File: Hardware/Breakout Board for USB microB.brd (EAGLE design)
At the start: 20.3 x 11.4 mm, 7 parts

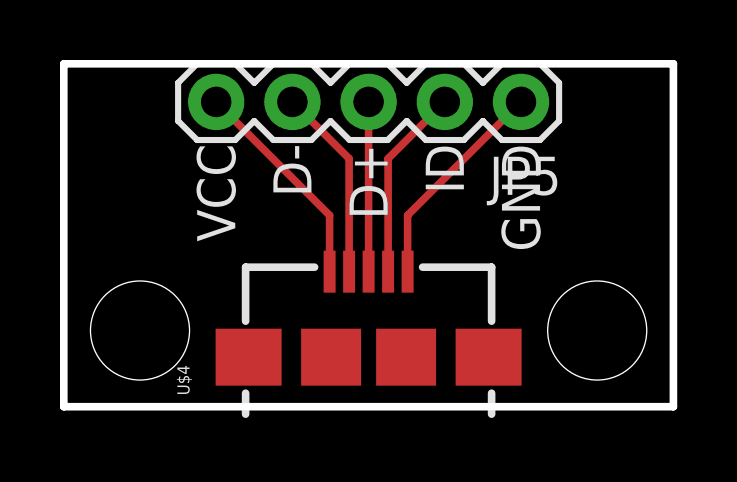
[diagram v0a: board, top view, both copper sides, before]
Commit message: Swapped in new microB FP w/ bosses
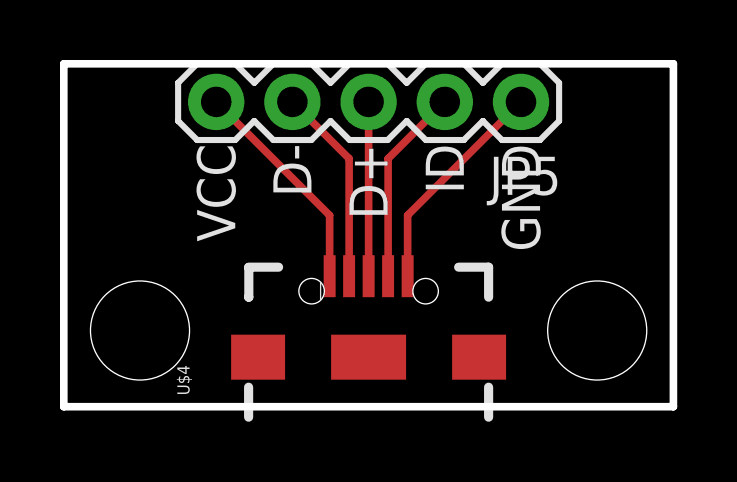
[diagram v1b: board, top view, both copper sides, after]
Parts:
- U$4: value USB_AB -> (none); device SparkFun-Connectors:USB-AB-MICRO-SMD -> Testing:USB-AB-MICRO-SMD_V02_BOSS
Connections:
- net D+: now also U$4.D+1; no longer U$4.D+
- net D-: now also U$4.D-1; no longer U$4.D-
- net GND: now also U$4.GND1; no longer U$4.GND
- net ID: now also U$4.ID1; no longer U$4.ID
- net VBUS: now also U$4.VBUS1; no longer U$4.VBUS

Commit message: Updated board with current FP.
No changes to layout just part value update. Engineering file audit. See
eagle issues for more info.
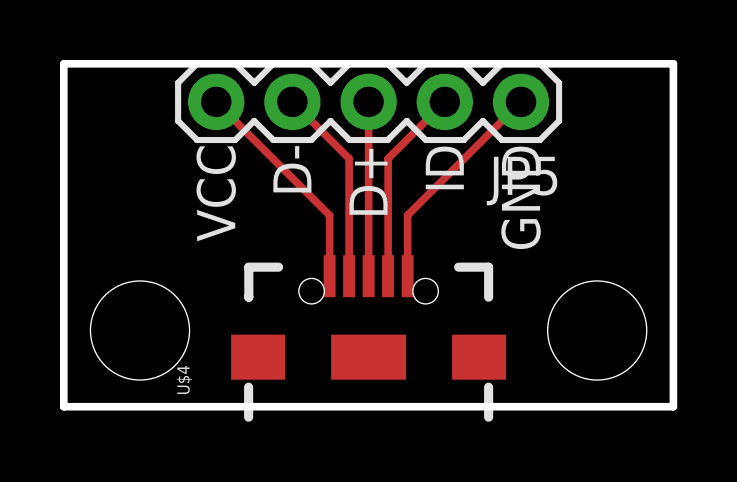
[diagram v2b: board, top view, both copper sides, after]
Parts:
- U$4: device Testing:USB-AB-MICRO-SMD_V02_BOSS -> SparkFun-Connectors:USB-AB-MICRO-SMD_V03
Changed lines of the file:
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@@
 <?xml version="1.0" encoding="utf-8"?>
 <!DOCTYPE eagle SYSTEM "eagle.dtd">
-<eagle version="6.4">
+<eagle version="7.2.0">
 <drawing>
 <settings>
@@
 <layer number="54" name="bGND_GNDA" color="1" fill="9" visible="no" active="no"/>
 <layer number="56" name="wert" color="7" fill="1" visible="no" active="yes"/>
+<layer number="57" name="tCAD" color="7" fill="1" visible="no" active="no"/>
+<layer number="90" name="Modules" color="5" fill="1" visible="no" active="no"/>
 <layer number="91" name="Nets" color="2" fill="1" visible="no" active="no"/>
 <layer number="92" name="Busses" color="1" fill="1" visible="no" active="no"/>
@@
 <layer number="97" name="Info" color="7" fill="1" visible="no" active="no"/>
 <layer number="98" name="Guide" color="6" fill="1" visible="no" active="no"/>
+<layer number="99" name="SpiceOrder" color="7" fill="1" visible="no" active="no"/>
 <layer number="100" name="Muster" color="7" fill="1" visible="no" active="no"/>
 <layer number="101" name="Patch_Top" color="12" fill="4" visible="no" active="yes"/>
@@
 <layer number="108" name="tplace-old" color="10" fill="1" visible="no" active="yes"/>
 <layer number="109" name="ref-old" color="11" fill="1" visible="no" active="yes"/>
+<layer number="110" name="fp0" color="7" fill="1" visible="yes" active="yes"/>
+<layer number="111" name="LPC17xx" color="7" fill="1" visible="yes" active="yes"/>
+<layer number="112" name="tSilk" color="7" fill="1" visible="yes" active="yes"/>
+<layer number="113" name="IDFDebug" color="4" fill="1" visible="yes" active="yes"/>
 <layer number="116" name="Patch_BOT" color="9" fill="4" visible="no" active="yes"/>
 <layer number="121" name="_tsilk" color="7" fill="1" visible="no" active="yes"/>
 <layer number="122" name="_bsilk" color="7" fill="1" visible="no" active="yes"/>
+<layer number="123" name="tTestmark" color="7" fill="1" visible="yes" active="yes"/>
+<layer number="124" name="bTestmark" color="7" fill="1" visible="yes" active="yes"/>
 <layer number="125" name="_tNames" color="7" fill="1" visible="no" active="yes"/>
+<layer number="126" name="_bNames" color="7" fill="1" visible="yes" active="yes"/>
+<layer number="127" name="_tValues" color="7" fill="1" visible="yes" active="yes"/>
+<layer number="128" name="_bValues" color="7" fill="1" visible="yes" active="yes"/>
+<layer number="131" name="tAdjust" color="7" fill="1" visible="yes" active="yes"/>
+<layer number="132" name="bAdjust" color="7" fill="1" visible="yes" active="yes"/>
 <layer number="144" name="Drill_legend" color="7" fill="1" visible="no" active="yes"/>
+<layer number="150" name="Notes" color="7" fill="1" visible="yes" active="yes"/>
 <layer number="151" name="HeatSink" color="7" fill="1" visible="no" active="yes"/>
+<layer number="152" name="_bDocu" color="7" fill="1" visible="yes" active="yes"/>
+<layer number="153" name="FabDoc1" color="7" fill="1" visible="yes" active="yes"/>
+<layer number="154" name="FabDoc2" color="7" fill="1" visible="yes" active="yes"/>
+<layer number="155" name="FabDoc3" color="7" fill="1" visible="yes" active="yes"/>
 <layer number="199" name="Contour" color="7" fill="1" visible="no" active="yes"/>
 <layer number="200" name="200bmp" color="1" fill="10" visible="no" active="yes"/>
@@
 <layer number="223" name="223bmp" color="24" fill="1" visible="no" active="no"/>
 <layer number="224" name="224bmp" color="25" fill="1" visible="no" active="no"/>
+<layer number="248" name="Housing" color="7" fill="1" visible="yes" active="yes"/>
+<layer number="249" name="Edge" color="7" fill="1" visible="yes" active="yes"/>
 <layer number="250" name="Descript" color="3" fill="1" visible="no" active="no"/>
 <layer number="251" name="SMDround" color="12" fill="11" visible="no" active="no"/>
@@
 <pass name="Default">
 <param name="RoutingGrid" value="50mil"/>
+<param name="AutoGrid" value="1"/>
+<param name="Efforts" value="0"/>
+<param name="TopRouterVariant" value="1"/>
 <param name="tpViaShape" value="round"/>
 <param name="PrefDir.1" value="|"/>
@@
 <element name="U$2" library="SparkFun-Aesthetics" package="CREATIVE_COMMONS" value="CREATIVE_COMMONS" x="21.59" y="-8.89"/>
 <element name="U$3" library="SparkFun-Aesthetics" package="OSHW-LOGO-S" value="OSHW-LOGOS" x="12.7" y="5.461" rot="MR0"/>
-<element name="U$4" library="Testing" package="USB-AB-MICRO-SMD_V02_BOSS" value="" x="10.16" y="1.651" rot="R90"/>
+<element name="U$4" library="SparkFun-Connectors" package="USB-AB-MICRO-SMD_V03" value="" x="10.16" y="1.651" rot="R90">
+<attribute name="PROD_ID" value="CONN-11794" x="10.16" y="1.651" size="1.778" layer="27" rot="R90" display="off"/>
+</element>
 </elements>
 <signals>

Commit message: Input Value
Added value to MICRO AB USB component for 3D Modeling
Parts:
- U$4: value (none) -> MICRO_AB_USB
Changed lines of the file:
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@@
 <?xml version="1.0" encoding="utf-8"?>
 <!DOCTYPE eagle SYSTEM "eagle.dtd">
-<eagle version="7.2.0">
+<eagle version="7.7.0">
 <drawing>
 <settings>
@@
 <element name="U$2" library="SparkFun-Aesthetics" package="CREATIVE_COMMONS" value="CREATIVE_COMMONS" x="21.59" y="-8.89"/>
 <element name="U$3" library="SparkFun-Aesthetics" package="OSHW-LOGO-S" value="OSHW-LOGOS" x="12.7" y="5.461" rot="MR0"/>
-<element name="U$4" library="SparkFun-Connectors" package="USB-AB-MICRO-SMD_V03" value="" x="10.16" y="1.651" rot="R90">
+<element name="U$4" library="SparkFun-Connectors" package="USB-AB-MICRO-SMD_V03" value="MICRO_AB_USB" x="10.16" y="1.651" rot="R90">
 <attribute name="PROD_ID" value="CONN-11794" x="10.16" y="1.651" size="1.778" layer="27" rot="R90" display="off"/>
 </element>
